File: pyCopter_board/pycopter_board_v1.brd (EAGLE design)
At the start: 81 x 80 mm, 36 parts, among them Q1 32.768kHz, U1 BNO055, U3 BMP180

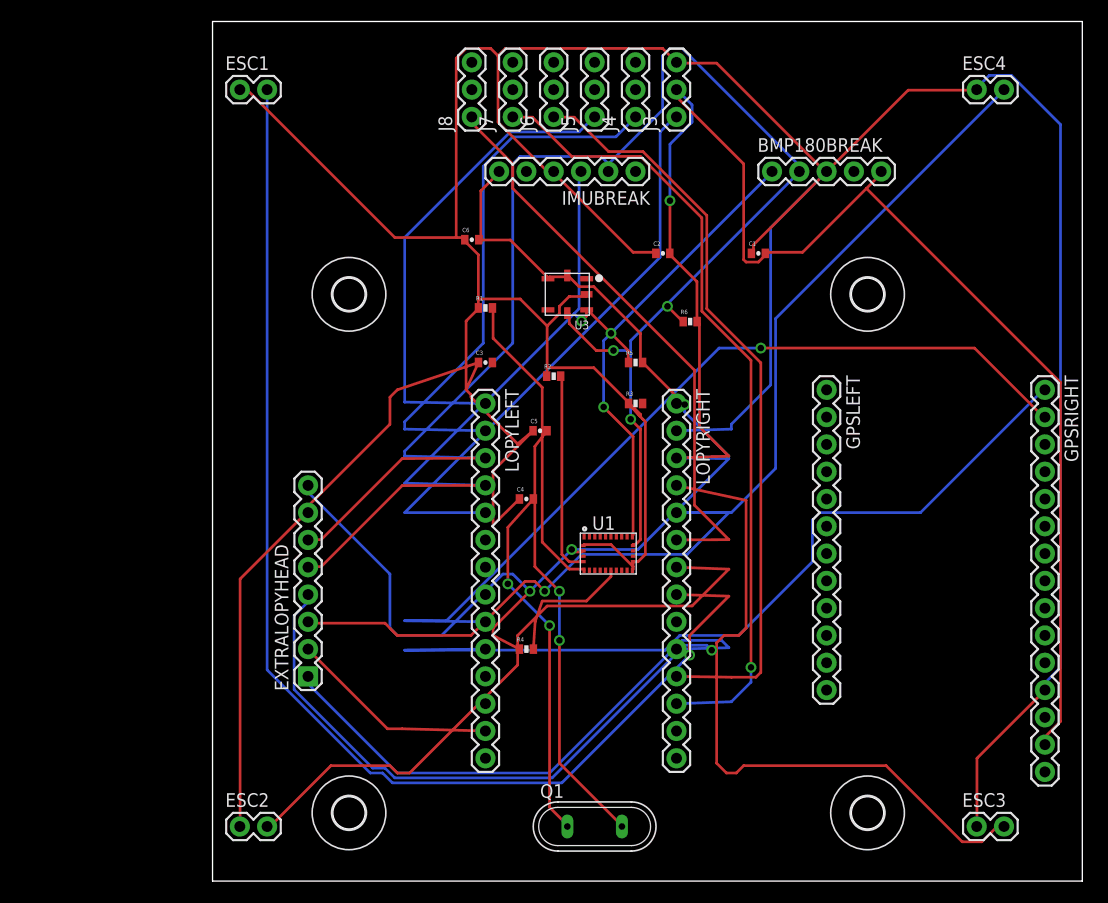
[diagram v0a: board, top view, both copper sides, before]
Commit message: added ground plane and made ESCs into triple headers.
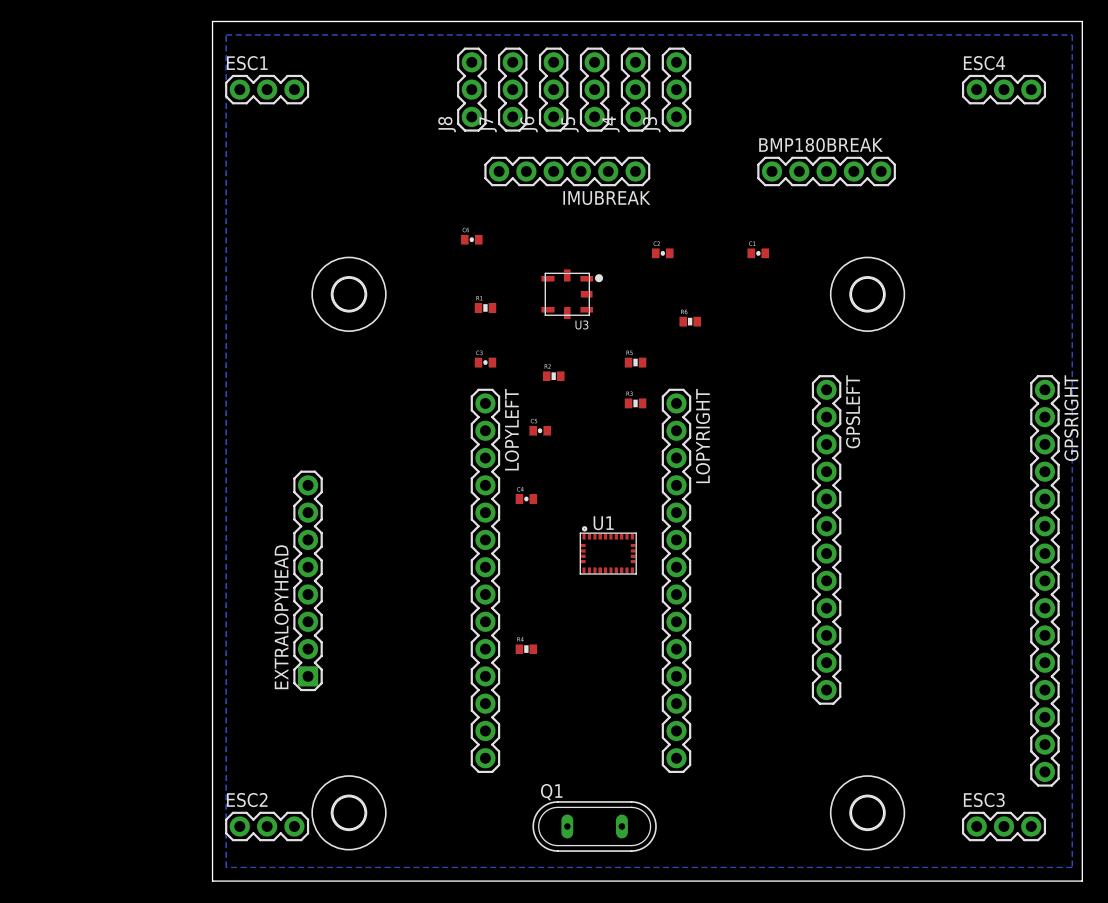
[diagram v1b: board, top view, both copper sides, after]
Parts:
- ESC1, ESC2, ESC3, ESC4: device SparkFun-Connectors:1X02 -> SparkFun-Connectors:1X03
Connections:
- new net N$10: ESC2.3
- new net N$8: ESC4.3
- net P19: now also ESC1.3; no longer ESC1.2
- net P20: now also ESC3.3; no longer ESC2.2
- net P22: no longer ESC4.2
- net P23: no longer ESC3.2
- net VIN: now also ESC1.2, ESC2.2, ESC3.2, ESC4.2
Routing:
- net GND: track 396.6 -> 0.00 mm
- net 3.3V: track 254.3 -> 0.00 mm, vias 4 -> 0
- net SCL: track 152.0 -> 0.00 mm, vias 3 -> 0
- net P23: track 121.4 -> 0.00 mm, vias 1 -> 0
- net P19: track 114.5 -> 0.00 mm, vias 1 -> 0
- net SDA: track 113.3 -> 0.00 mm, vias 3 -> 0
- net P22: track 105.1 -> 0.00 mm, vias 1 -> 0
- net GPS_RX: track 80.3 -> 0.00 mm, vias 1 -> 0
- net GPS_TX: track 79.4 -> 0.00 mm
- net GEAR: track 74.3 -> 0.00 mm, vias 1 -> 0
- net RUDD: track 70.7 -> 0.00 mm
- net P20: track 60.1 -> 0.00 mm
- net THRO: track 54.9 -> 0.00 mm
- net AUX1: track 54.2 -> 0.00 mm
- net P17: track 53.6 -> 0.00 mm
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- added copper zone on layer 16, net GND

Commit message: started adding traces to board. Added all GND traces and VIN traces. Working on 3.3v now.
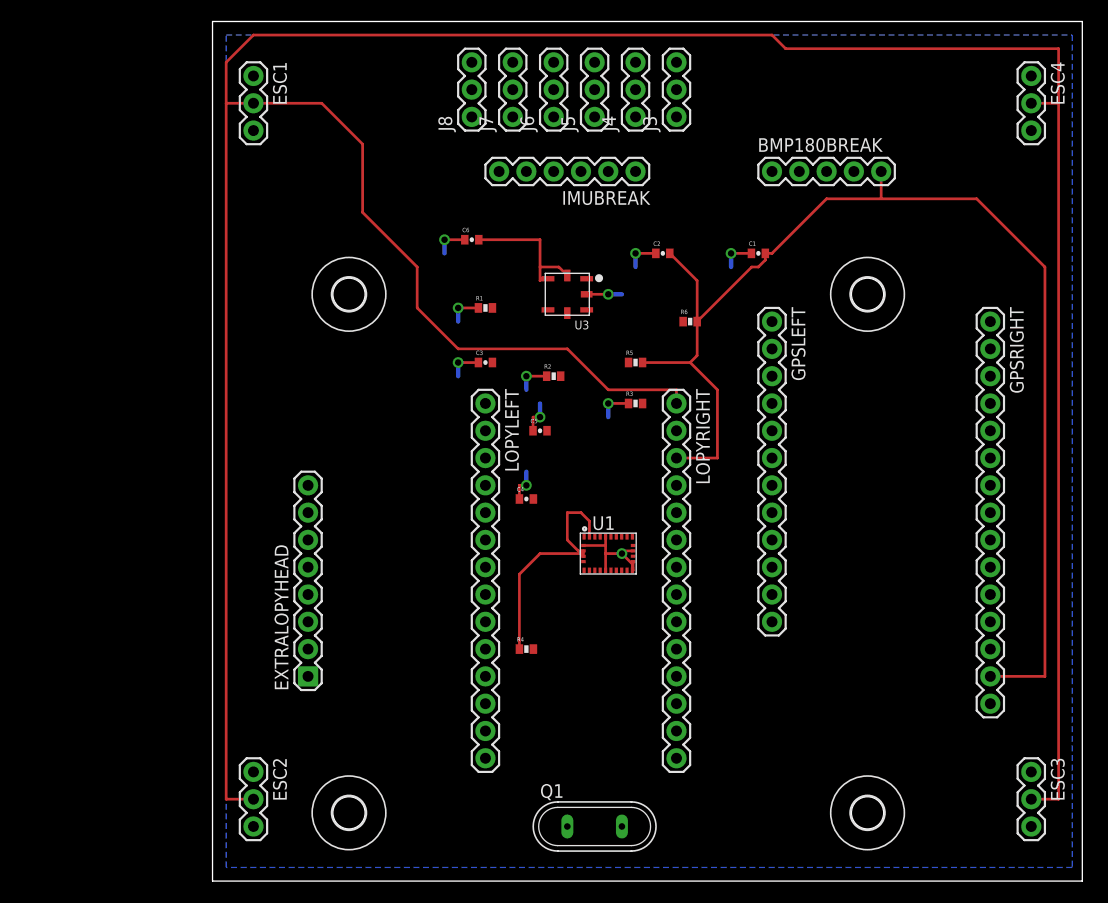
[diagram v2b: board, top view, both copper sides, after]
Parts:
- moved GPSLEFT 8.13 mm to (69.8, 52.1)
- moved GPSRIGHT 8.13 mm to (90.2, 52.1)
- moved ESC3 7.18 mm to (94.0, 10.2), turned to 270 degrees
- moved ESC4 5.24 mm to (94.0, 74.9), turned to 270 degrees
- moved ESC2 5.24 mm to (21.6, 10.2), turned to 270 degrees
- moved ESC1 1.80 mm to (21.6, 74.9), turned to 270 degrees
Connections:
- removed net N$10: ESC2.3
- removed net N$8: ESC4.3
- net P20: now also ESC2.3; no longer ESC3.3
- net P22: now also ESC4.3
- net P23: now also ESC3.3
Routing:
- net VIN: track 0.00 -> 285.3 mm
- net 3.3V: track 0.00 -> 151.3 mm
- net GND: track 0.00 -> 43.7 mm, vias 0 -> 11

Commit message: board is all connected as is. Will try for another version in the morning which has more components on the bottom.
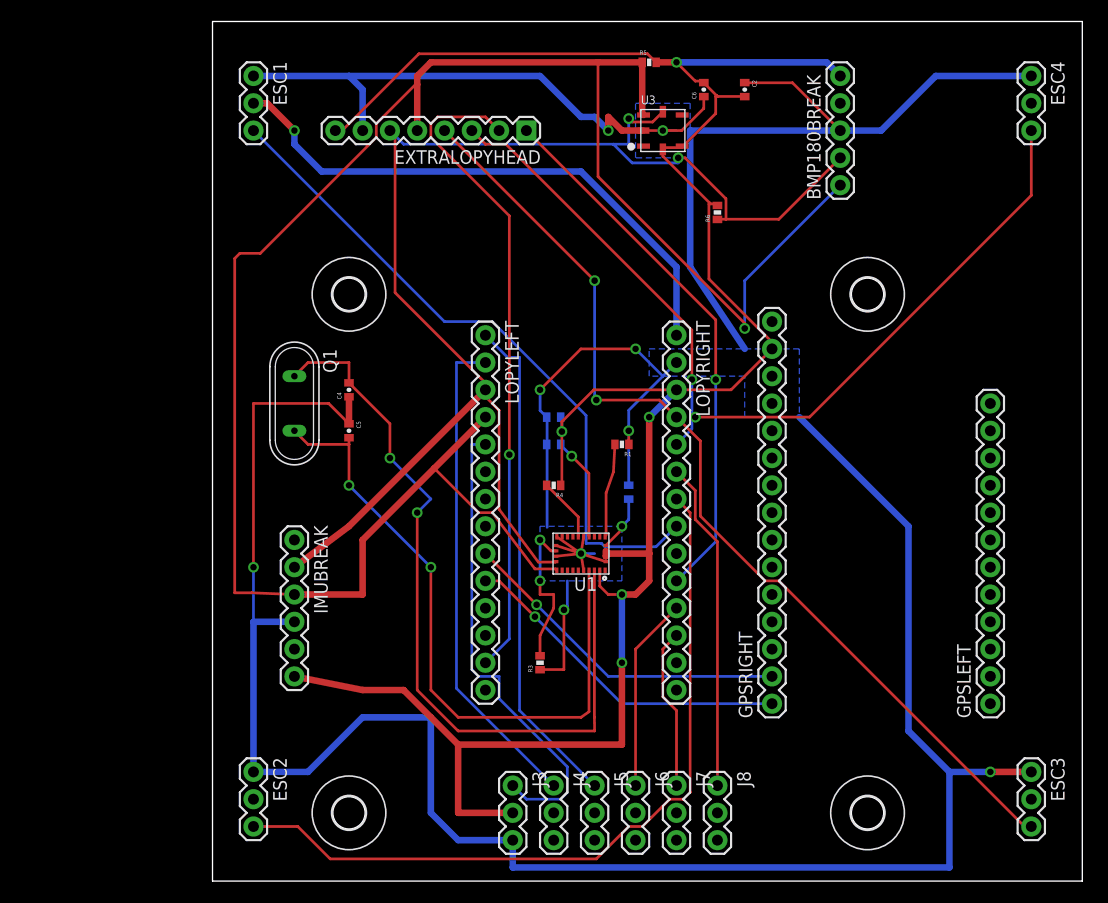
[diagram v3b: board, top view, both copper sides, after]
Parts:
- moved J8 66.3 mm to (64.8, 8.89), turned to 270 degrees
- moved J3 64.1 mm to (45.7, 8.89), turned to 270 degrees
- moved J7 64.1 mm to (61.0, 8.89), turned to 270 degrees
- moved J4 62.7 mm to (49.5, 8.89), turned to 270 degrees
- moved J6 62.7 mm to (57.1, 8.89), turned to 270 degrees
- moved J5 62.2 mm to (53.3, 8.89), turned to 270 degrees
- moved EXTRALOPYHEAD 54.7 mm to (47.0, 69.8), turned to 180 degrees
- moved Q1 48.3 mm to (25.4, 44.5), turned to 270 degrees
- moved IMUBREAK 46.7 mm to (25.4, 31.8), turned to 270 degrees
- moved GPSLEFT 41.0 mm to (90.2, 16.5), turned to 90 degrees
- moved GPSRIGHT 41.0 mm to (69.8, 16.5), turned to 90 degrees
- moved R5 28.0 mm to (58.4, 76.2)
- moved C6 25.7 mm to (63.5, 73.7), turned to 90 degrees
- moved R3 25.7 mm to (48.3, 20.3), turned to 90 degrees
- moved C1 24.4 mm to (49.5, 43.2), flipped to the bottom, turned to 180 degrees
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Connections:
- removed net N$7: BMP180BREAK.4
- removed net N$9: LOPYRIGHT.9
- net VIN: no longer ESC2.2, ESC3.2, ESC4.2
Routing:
- net GND: track 43.7 -> 372.7 mm, vias 11 -> 9
- net VIN: track 285.3 -> 52.8 mm, vias 0 -> 1
- net SDA: track 0.00 -> 183.4 mm, vias 0 -> 1
- net SCL: track 0.00 -> 129.5 mm, vias 0 -> 2
- net P23: track 0.00 -> 92.0 mm, vias 0 -> 2
- net P22: track 0.00 -> 85.6 mm, vias 0 -> 2
- net XIN: track 0.00 -> 72.8 mm, vias 0 -> 2
- net P20: track 0.00 -> 72.3 mm
- net P19: track 0.00 -> 63.2 mm
- net XOUT: track 0.00 -> 61.3 mm, vias 0 -> 2
- net P0: track 0.00 -> 61.2 mm, vias 0 -> 1
- net 3.3V: track 151.3 -> 208.6 mm, vias 0 -> 5
- net P17: track 0.00 -> 50.7 mm, vias 0 -> 1
- net ELEV: track 0.00 -> 46.8 mm
- net AILE: track 0.00 -> 45.8 mm
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
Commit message: at a good base point for autorouter. The power traces are all thicker, and routed the all the radio transmitter pins to the outside of the LoPy.
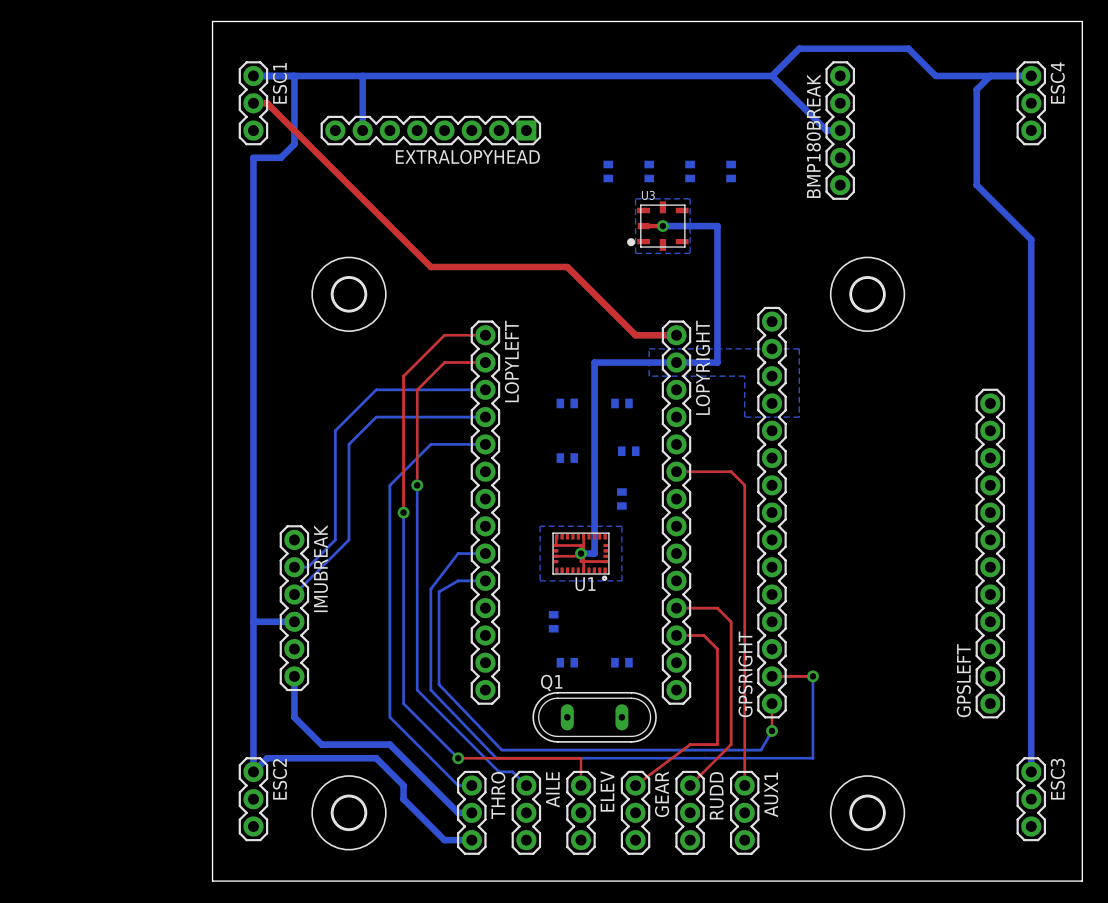
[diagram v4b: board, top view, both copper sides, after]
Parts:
- removed J3, J4, J5, J7, J8: (no value), SparkFun-Connectors:1X03
- added AILE, AUX1, ELEV, RUDD, THRO: (no value), SparkFun-Connectors:1X03
- moved Q1 40.4 mm to (53.3, 15.2), turned to 0 degrees
- moved C5 33.3 mm to (55.9, 20.3), flipped to the bottom, turned to 0 degrees
- moved C4 32.5 mm to (50.8, 20.3), flipped to the bottom, turned to 180 degrees
- moved R5 10.9 mm to (54.6, 66.0), flipped to the bottom, turned to 90 degrees
- moved C2 9.16 mm to (62.2, 66.0), flipped to the bottom, turned to 90 degrees
- moved C6 9.16 mm to (58.4, 66.0), flipped to the bottom
- moved U3 8.89 mm to (59.7, 61.0)
- moved R4 6.48 mm to (55.9, 35.6), flipped to the bottom, turned to 90 degrees
- moved R6 4.02 mm to (66.0, 66.0), flipped to the bottom, turned to 270 degrees
- moved R3 4.02 mm to (49.5, 24.1), flipped to the bottom
- moved R1 3.81 mm to (55.9, 44.5), flipped to the bottom
- moved R2 3.81 mm to (56.5, 40.0), turned to 180 degrees
- moved C1 1.80 mm to (50.8, 44.5), turned to 0 degrees
- moved C3 1.80 mm to (50.8, 39.4), turned to 0 degrees
- renumbered J6 to GEAR
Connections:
- net 3.3V: now also THRO.2; no longer J3.2
- net AILE: now also AILE.1; no longer J4.1
- net AUX1: now also AUX1.1; no longer J8.1
- net ELEV: now also ELEV.1; no longer J5.1
- net GEAR: now also GEAR.1; no longer J7.1
- net GND: now also THRO.3; no longer J3.3
- net RUDD: now also RUDD.1; no longer GEAR.1
- net THRO: now also THRO.1; no longer J3.1
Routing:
- net 3.3V: track 208.6 -> 24.0 mm, vias 5 -> 0
- net SDA: track 183.4 -> 29.8 mm, vias 1 -> 0
- net SCL: track 129.5 -> 30.6 mm, vias 2 -> 0
- net P23: track 92.0 -> 0.00 mm, vias 2 -> 0
- net P22: track 85.6 -> 0.00 mm, vias 2 -> 0
- net XIN: track 72.8 -> 0.00 mm, vias 2 -> 0
- net P20: track 72.3 -> 0.00 mm
- net P19: track 63.2 -> 0.00 mm
- net XOUT: track 61.3 -> 0.00 mm, vias 2 -> 0
- net P0: track 61.2 -> 0.00 mm, vias 1 -> 0
- net P17: track 50.7 -> 0.00 mm, vias 1 -> 0
- net GND: track 372.7 -> 323.8 mm, vias 9 -> 2
- net GPS_RX: track 31.4 -> 65.8 mm
- net GPS_TX: track 31.4 -> 50.4 mm
- net N$2: track 14.3 -> 0.00 mm, vias 2 -> 0
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
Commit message: added a large ground layer after the fact to what should be the final board revision. just need to add rounded edges for the dimensions.
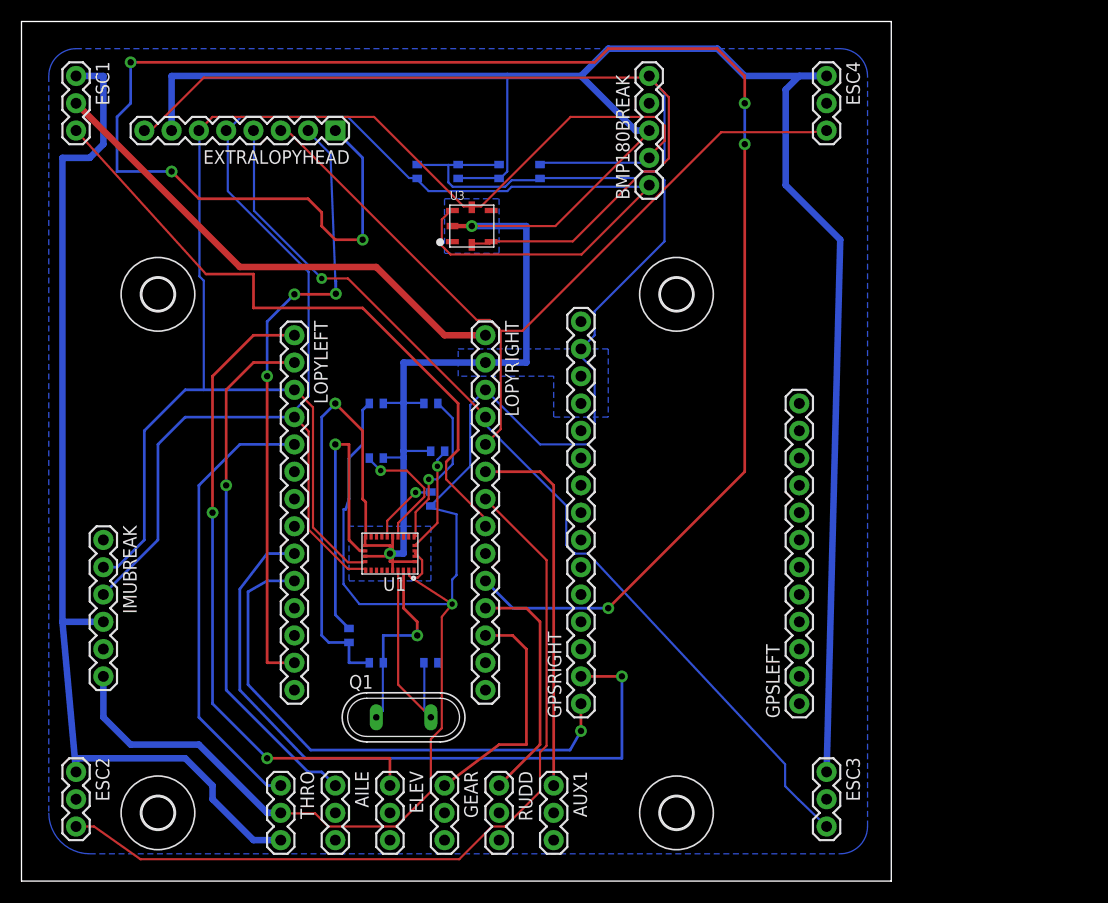
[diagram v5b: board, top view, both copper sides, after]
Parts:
- moved R3 19.1 mm to (30.5, 22.9)
- moved ESC3 19.0 mm to (74.9, 10.2)
- moved ESC4 19.0 mm to (74.9, 74.9)
- moved R6 17.8 mm to (48.3, 66.0)
- moved AILE 17.8 mm to (29.2, 8.89)
- moved AUX1 17.8 mm to (49.5, 8.89)
- moved BMP180BREAK 17.8 mm to (58.4, 64.8)
- moved C5 17.8 mm to (38.1, 20.3)
- moved C6 17.8 mm to (40.6, 66.0)
- moved ELEV 17.8 mm to (34.3, 8.89)
- moved EXTRALOPYHEAD 17.8 mm to (29.2, 69.8)
- moved GEAR 17.8 mm to (39.4, 8.89)
- moved GPSLEFT 17.8 mm to (72.4, 16.5)
- moved H5 17.8 mm to (12.7, 6.35)
- moved H7 17.8 mm to (12.7, 54.6)
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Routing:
- net 3.3V: track 24.0 -> 280.2 mm, vias 0 -> 1
- net P17: track 0.00 -> 174.1 mm, vias 0 -> 6
- net SDA: track 29.8 -> 147.5 mm
- net SCL: track 30.6 -> 139.9 mm
- net P23: track 0.00 -> 88.7 mm, vias 0 -> 1
- net P22: track 0.00 -> 77.3 mm
- net P20: track 0.00 -> 76.6 mm
- net GND: track 323.8 -> 394.0 mm, vias 2 -> 3
- net P19: track 0.00 -> 61.7 mm
- net P0: track 0.00 -> 59.2 mm, vias 0 -> 3
- net N$2: track 0.00 -> 29.7 mm, vias 0 -> 1
- net XOUT: track 0.00 -> 20.3 mm
- net XIN: track 0.00 -> 17.7 mm, vias 0 -> 1
- net N$3: track 0.00 -> 15.0 mm, vias 0 -> 1
- net N$1: track 0.00 -> 11.9 mm, vias 0 -> 1
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
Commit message: changed the dimension of the board to have rounded corners. Now giving fonts and silkscreen some attention.
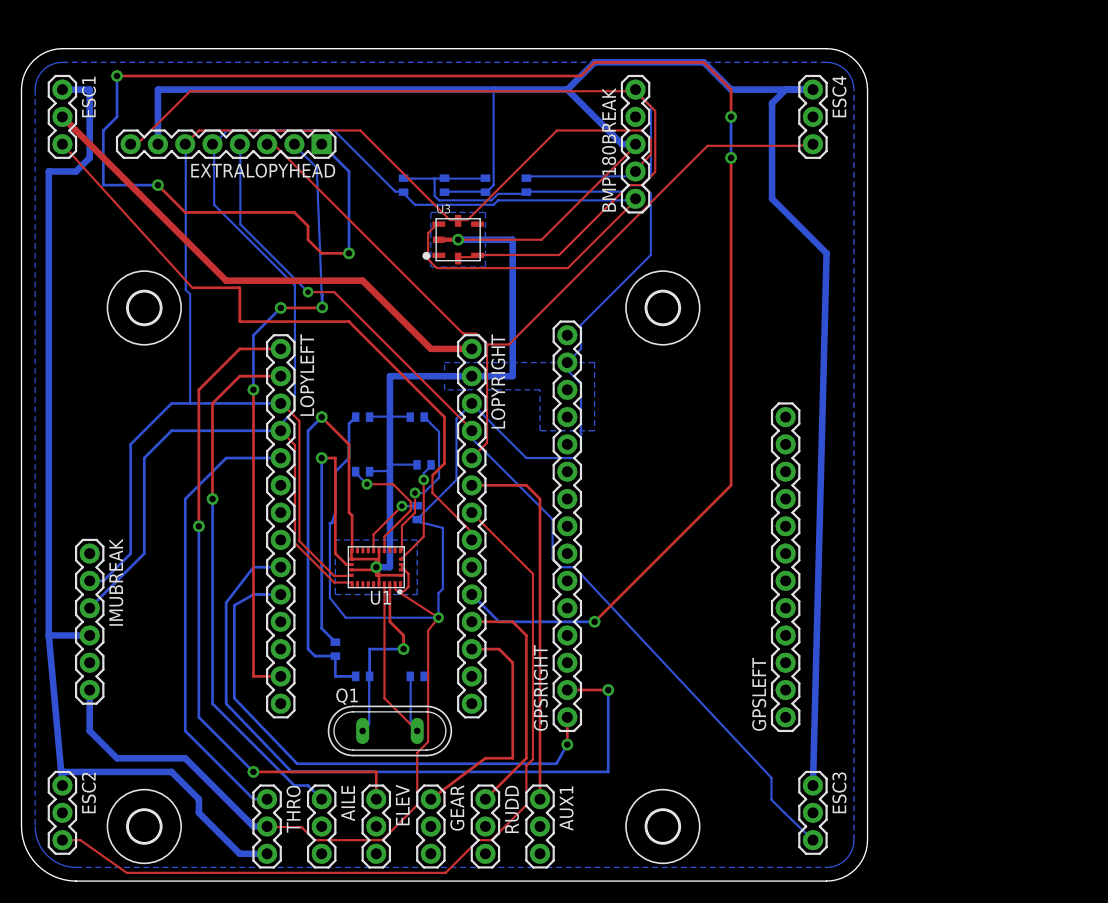
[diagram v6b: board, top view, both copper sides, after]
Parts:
- moved ESC4 1.80 mm to (73.7, 73.7)
- moved C2 1.80 mm to (43.2, 64.8)
- moved C6 1.80 mm to (39.4, 64.8)
- moved ESC1 1.80 mm to (3.81, 73.7)
- moved ESC3 1.80 mm to (73.7, 8.89)
- moved C1 1.80 mm to (31.8, 43.2)
- moved R1 1.80 mm to (36.8, 43.2)
- moved R4 1.80 mm to (36.8, 34.3)
- moved R5 1.80 mm to (35.6, 64.8)
- moved R6 1.80 mm to (47.0, 64.8)
- moved GPSRIGHT 1.80 mm to (50.8, 15.2)
- moved AUX1 1.80 mm to (48.3, 7.62)
- moved RUDD 1.80 mm to (43.2, 7.62)
- moved C4 1.80 mm to (31.8, 19.1)
- moved C5 1.80 mm to (36.8, 19.1)
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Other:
- board size 81 x 80 mm -> 78.7 x 77.5 mm
